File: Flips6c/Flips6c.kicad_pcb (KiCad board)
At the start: 2 copper layers, 90 x 50 mm, 20 parts, among them CN1 Conn_02x04_Odd_Even, U1 74HCT595, U2 74HCT595, U3 74HCT595

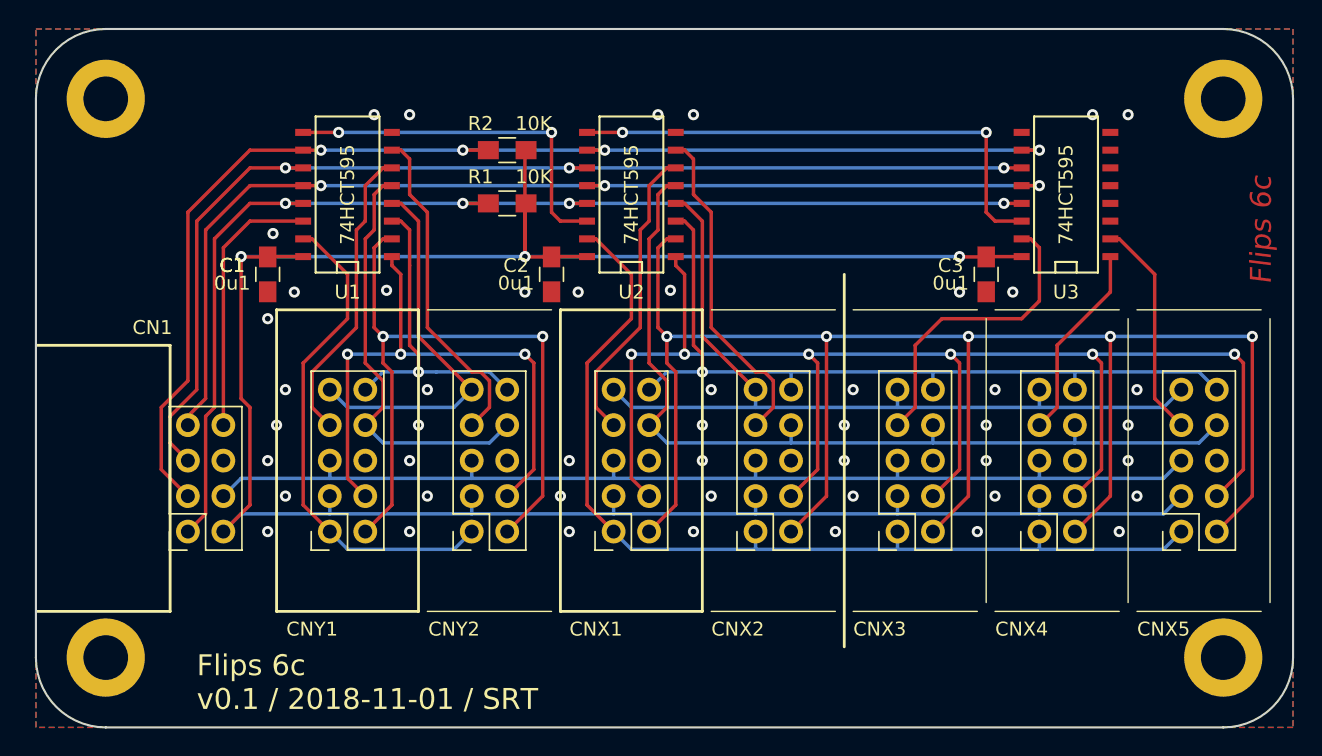
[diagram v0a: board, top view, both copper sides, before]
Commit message: changing trace widths
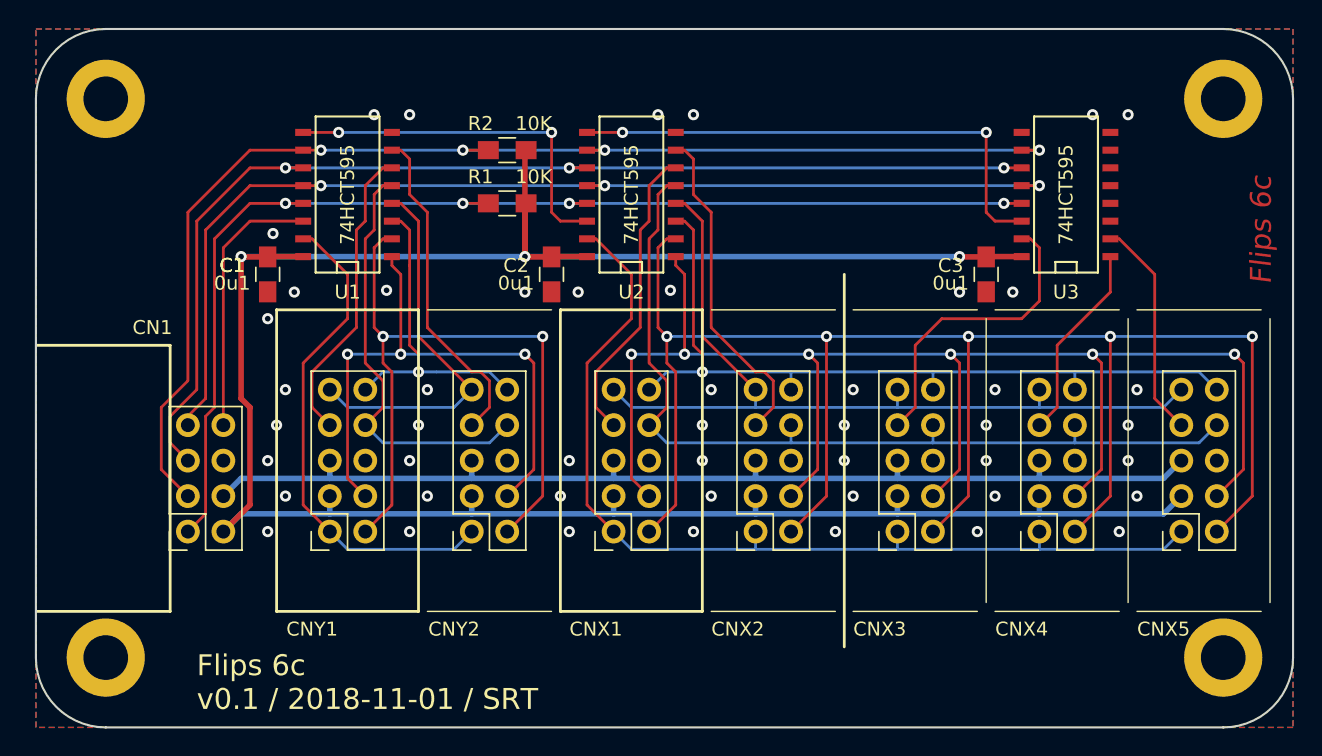
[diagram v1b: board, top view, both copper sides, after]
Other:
- net class Default: trace_width 0.25 -> 0.2
- net class POW added: clearance 0.2, trace_width 0.4, via_dia 0.8, via_drill 0.4

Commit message: flips 6c to use own UFP2810 connector
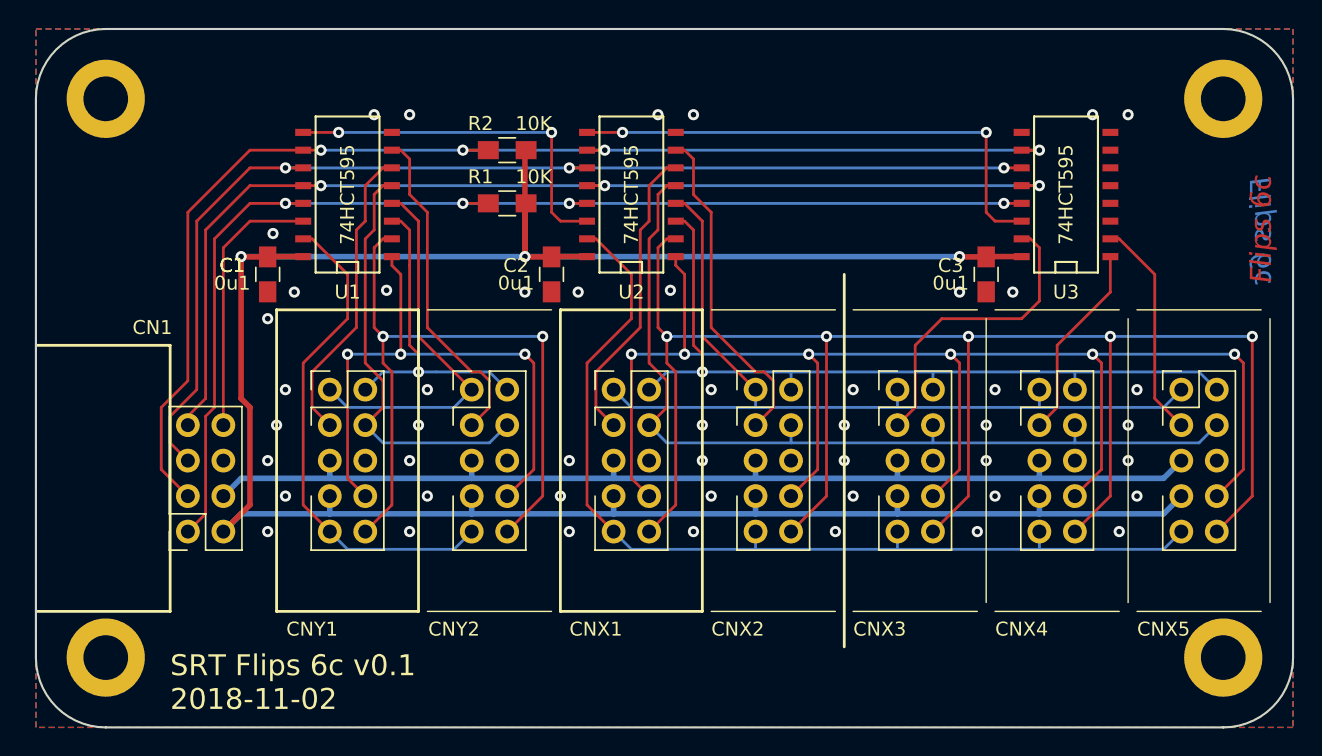
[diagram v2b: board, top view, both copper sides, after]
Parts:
- CNX1, CNX2, CNX3, CNX4, CNX5, CNY1, CNY2: value Conn_02x05_Odd_Even -> UFP2810; footprint Socket_Strips:Socket_Strip_Straight_2x05_Pitch2.54mm -> Own:Pin_Header_Straight_Shrouded_2x05_Pitch2.54mm
- moved CNX1 10.2 mm to (213.4, 83.8), turned to 0 degrees
- moved CNX2 10.2 mm to (223.5, 83.8), turned to 0 degrees
- moved CNX3 10.2 mm to (233.7, 83.8), turned to 0 degrees
- moved CNX4 10.2 mm to (243.8, 83.8), turned to 0 degrees
- moved CNX5 10.2 mm to (254.0, 83.8), turned to 0 degrees
- moved CNY1 10.2 mm to (193.0, 83.8), turned to 0 degrees
- moved CNY2 10.2 mm to (203.2, 83.8), turned to 0 degrees
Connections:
- CNX1 pad 1: /XA.0 -> /XB.1
- CNX1 pad 10: /XB.0 -> /XA.2
- CNX1 pad 2: /XA.2 -> /XB.0
- CNX1 pad 3: +5V -> /XEN1
- CNX1 pad 4: /XA.1 -> /XDAT
- CNX1 pad 7: /XEN1 -> +5V
- CNX1 pad 8: /XDAT -> /XA.1
- CNX1 pad 9: /XB.1 -> /XA.0
- CNX2 pad 1: /XA.0 -> /XB.1
- CNX2 pad 10: /XB.0 -> /XA.2
- CNX2 pad 2: /XA.2 -> /XB.0
- CNX2 pad 3: +5V -> /XEN2
- CNX2 pad 4: /XA.1 -> /XDAT
- CNX2 pad 7: /XEN2 -> +5V
- CNX2 pad 8: /XDAT -> /XA.1
- CNX2 pad 9: /XB.1 -> /XA.0
- CNX3 pad 1: /XA.0 -> /XB.1
- CNX3 pad 10: /XB.0 -> /XA.2
- CNX3 pad 2: /XA.2 -> /XB.0
- CNX3 pad 3: +5V -> /XEN3
- CNX3 pad 4: /XA.1 -> /XDAT
- CNX3 pad 7: /XEN3 -> +5V
- CNX3 pad 8: /XDAT -> /XA.1
- CNX3 pad 9: /XB.1 -> /XA.0
- CNX4 pad 1: /XA.0 -> /XB.1
- CNX4 pad 10: /XB.0 -> /XA.2
- CNX4 pad 2: /XA.2 -> /XB.0
- CNX4 pad 3: +5V -> /XEN4
- CNX4 pad 4: /XA.1 -> /XDAT
- CNX4 pad 7: /XEN4 -> +5V
- CNX4 pad 8: /XDAT -> /XA.1
- CNX4 pad 9: /XB.1 -> /XA.0
- CNX5 pad 1: /XA.0 -> /XB.1
- CNX5 pad 10: /XB.0 -> /XA.2
- CNX5 pad 2: /XA.2 -> /XB.0
- CNX5 pad 3: +5V -> /XEN5
- CNX5 pad 4: /XA.1 -> /XDAT
- CNX5 pad 7: /XEN5 -> +5V
- CNX5 pad 8: /XDAT -> /XA.1
- CNX5 pad 9: /XB.1 -> /XA.0
- CNY1 pad 1: /YA.0 -> /YB.1
- CNY1 pad 10: /YB.0 -> /YA.2
- CNY1 pad 2: /YA.2 -> /YB.0
- CNY1 pad 3: +5V -> /YEN1
- CNY1 pad 4: /YA.1 -> /YDAT
- CNY1 pad 7: /YEN1 -> +5V
- CNY1 pad 8: /YDAT -> /YA.1
- CNY1 pad 9: /YB.1 -> /YA.0
- CNY2 pad 1: /YA.0 -> /YB.1
- CNY2 pad 10: /YB.0 -> /YA.2
- CNY2 pad 2: /YA.2 -> /YB.0
- CNY2 pad 3: +5V -> /YEN2
- CNY2 pad 4: /YA.1 -> /YDAT
- CNY2 pad 7: /YEN2 -> +5V
- CNY2 pad 8: /YDAT -> /YA.1
- CNY2 pad 9: /YB.1 -> /YA.0
- U3 pad 3: (no net) -> /XEN6
- U3 pad 4: (no net) -> /XEN7
- U3 pad 5: (no net) -> /XEN8
- U3 pad 6: (no net) -> /YEN3
- U3 pad 7: (no net) -> /YEN4
- U3 pad 9: (no net) -> Net-(U3-Pad9)
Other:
- board text added: "SRT Flips 6c v0.1 2018-11-02"
- board text removed: "Flips 6c v0.1 / 2018-11-01 / SRT"

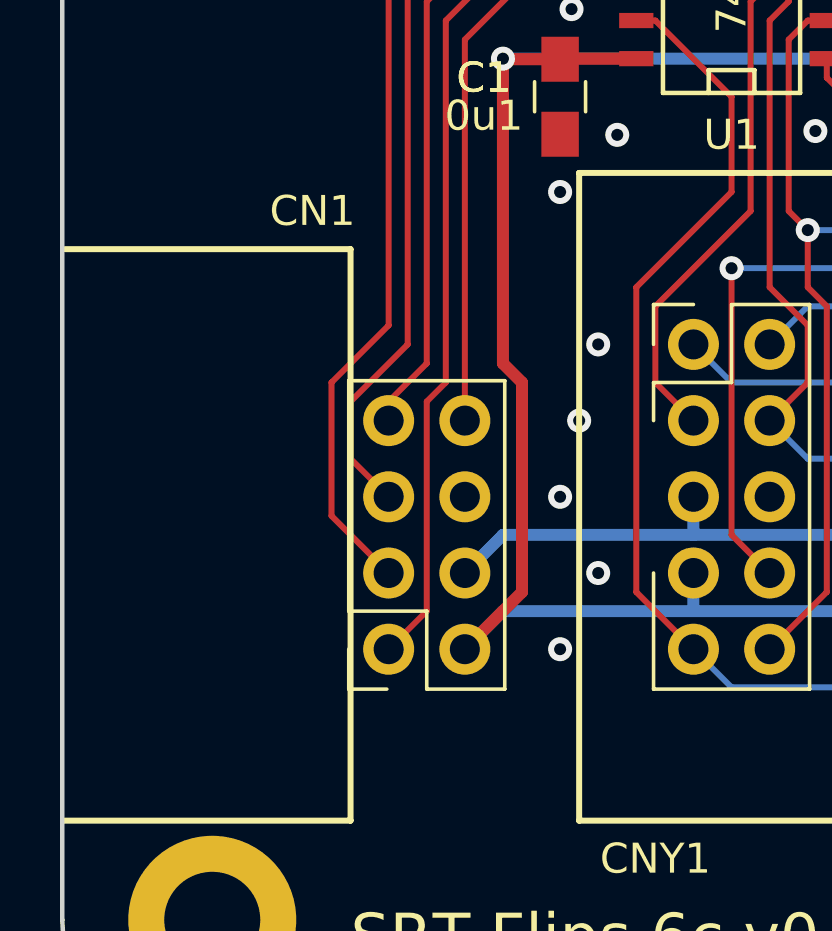
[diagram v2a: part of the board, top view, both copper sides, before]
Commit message: fixing 8 pin connector
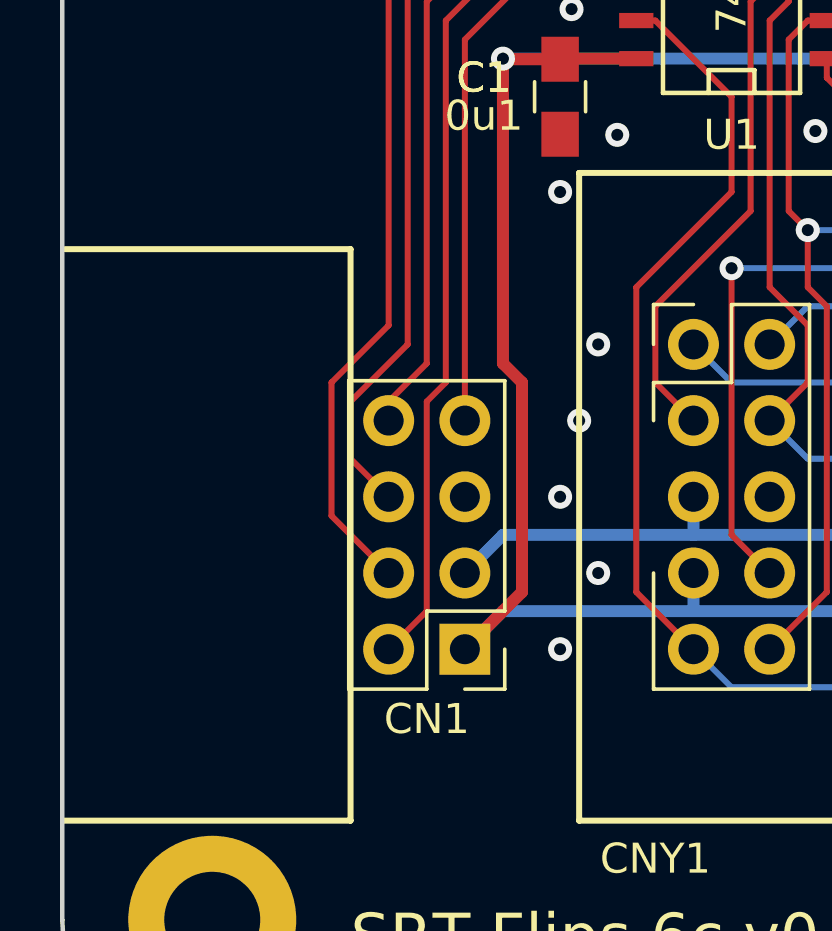
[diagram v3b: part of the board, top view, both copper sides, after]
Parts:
- CN1: footprint Socket_Strips:Socket_Strip_Straight_2x04_Pitch2.54mm -> Pin_Headers:Pin_Header_Straight_2x04_Pitch2.54mm
- moved CN1 2.54 mm to (185.4, 94.0)
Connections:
- CN1 pad 1: /~OE -> +5V
- CN1 pad 2: +5V -> /~OE
- CN1 pad 3: /~SRCLR -> +12V
- CN1 pad 4: +12V -> /~SRCLR
- CN1 pad 5: /SRCLK -> GND
- CN1 pad 6: GND -> /SRCLK
- CN1 pad 7: /RCLK -> /DIN
- CN1 pad 8: /DIN -> /RCLK
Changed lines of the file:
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@@
     (pad 1 thru_hole circle (at 0 0) (size 5.6 5.6) (drill 3.2) (layers *.Cu *.Mask))
-  )
-  (module Socket_Strips:Socket_Strip_Straight_2x04_Pitch2.54mm (layer F.Cu)
-    (at 182.88 93.98 180)
-    (descr "Through hole straight socket strip, 2x04, 2.54mm pitch, double rows")
-    (tags "Through hole socket strip THT 2x04 2.54mm double row")
-    (fp_text reference CN1 (at 2.54 14.605) (layer F.SilkS)
-      (effects (font (size 1 1) (thickness 0.15)))
-    )
-    (fp_text value Conn_02x04_Odd_Even (at -1.27 9.95 180) (layer F.Fab)
-      (effects (font (size 1 1) (thickness 0.15)))
-    )
-    (fp_text user %R (at 2.54 14.605 180) (layer F.Fab)
-      (effects (font (size 1 1) (thickness 0.15)))
-    )
-    (fp_line (start 1.8 -1.8) (end -4.35 -1.8) (layer F.CrtYd) (width 0.05))
-    (fp_line (start 1.8 9.4) (end 1.8 -1.8) (layer F.CrtYd) (width 0.05))
-    (fp_line (start -4.35 9.4) (end 1.8 9.4) (layer F.CrtYd) (width 0.05))
-    (fp_line (start -4.35 -1.8) (end -4.35 9.4) (layer F.CrtYd) (width 0.05))
-    (fp_line (start 1.33 -1.33) (end 0.06 -1.33) (layer F.SilkS) (width 0.12))
-    (fp_line (start 1.33 0) (end 1.33 -1.33) (layer F.SilkS) (width 0.12))
-    (fp_line (start -1.27 1.27) (end 1.33 1.27) (layer F.SilkS) (width 0.12))
-    (fp_line (start -1.27 -1.33) (end -1.27 1.27) (layer F.SilkS) (width 0.12))
-    (fp_line (start -3.87 -1.33) (end -1.27 -1.33) (layer F.SilkS) (width 0.12))
-    (fp_line (start -3.87 8.95) (end -3.87 -1.33) (layer F.SilkS) (width 0.12))
-    (fp_line (start 1.33 8.95) (end -3.87 8.95) (layer F.SilkS) (width 0.12))
-    (fp_line (start 1.33 1.27) (end 1.33 8.95) (layer F.SilkS) (width 0.12))
-    (fp_line (start 1.27 -1.27) (end -3.81 -1.27) (layer F.Fab) (width 0.1))
-    (fp_line (start 1.27 8.89) (end 1.27 -1.27) (layer F.Fab) (width 0.1))
-    (fp_line (start -3.81 8.89) (end 1.27 8.89) (layer F.Fab) (width 0.1))
-    (fp_line (start -3.81 -1.27) (end -3.81 8.89) (layer F.Fab) (width 0.1))
-    (pad 8 thru_hole oval (at -2.54 7.62 180) (size 1.7 1.7) (drill 1) (layers *.Cu *.Mask)
-      (net 4 /DIN))
-    (pad 7 thru_hole oval (at 0 7.62 180) (size 1.7 1.7) (drill 1) (layers *.Cu *.Mask)
-      (net 5 /RCLK))
-    (pad 6 thru_hole oval (at -2.54 5.08 180) (size 1.7 1.7) (drill 1) (layers *.Cu *.Mask)
-      (net 2 GND))
-    (pad 5 thru_hole oval (at 0 5.08 180) (size 1.7 1.7) (drill 1) (layers *.Cu *.Mask)
-      (net 6 /SRCLK))
-    (pad 4 thru_hole oval (at -2.54 2.54 180) (size 1.7 1.7) (drill 1) (layers *.Cu *.Mask)
-      (net 3 +12V))
-    (pad 3 thru_hole oval (at 0 2.54 180) (size 1.7 1.7) (drill 1) (layers *.Cu *.Mask)
-      (net 7 /~SRCLR))
-    (pad 2 thru_hole oval (at -2.54 0 180) (size 1.7 1.7) (drill 1) (layers *.Cu *.Mask)
-      (net 1 +5V))
-    (pad 1 thru_hole circle (at 0 0 180) (size 1.7 1.7) (drill 1) (layers *.Cu *.Mask)
-      (net 9 /~OE))
-    (model ${KISYS3DMOD}/Connector_IDC.3dshapes/IDC-Header_2x04_P2.54mm_Horizontal.wrl
-      (offset (xyz -2.54 0 0))
-      (scale (xyz 1 1 1))
-      (rotate (xyz 0 0 0))
-    )
   )
   (module Capacitors_SMD:C_0805_HandSoldering (layer F.Cu)
@@
       (at (xyz 0 0 0))
       (scale (xyz 1 1 1))
+      (rotate (xyz 0 0 0))
+    )
+  )
+  (module Pin_Headers:Pin_Header_Straight_2x04_Pitch2.54mm (layer F.Cu)
+    (at 185.42 93.98 180)
+    (descr "Through hole straight pin header, 2x04, 2.54mm pitch, double rows")
+    (tags "Through hole pin header THT 2x04 2.54mm double row")
+    (fp_text reference CN1 (at 1.27 -2.33 180) (layer F.SilkS)
+      (effects (font (size 1 1) (thickness 0.15)))
+    )
+    (fp_text value Conn_02x04_Odd_Even (at 1.27 9.95 180) (layer F.Fab)
+      (effects (font (size 1 1) (thickness 0.15)))
+    )
+    (fp_text user %R (at 1.27 3.81 270) (layer F.Fab)
+      (effects (font (size 1 1) (thickness 0.15)))
+    )
+    (fp_line (start 4.35 -1.8) (end -1.8 -1.8) (layer F.CrtYd) (width 0.05))
+    (fp_line (start 4.35 9.4) (end 4.35 -1.8) (layer F.CrtYd) (width 0.05))
+    (fp_line (start -1.8 9.4) (end 4.35 9.4) (layer F.CrtYd) (width 0.05))
+    (fp_line (start -1.8 -1.8) (end -1.8 9.4) (layer F.CrtYd) (width 0.05))
+    (fp_line (start -1.33 -1.33) (end 0 -1.33) (layer F.SilkS) (width 0.12))
+    (fp_line (start -1.33 0) (end -1.33 -1.33) (layer F.SilkS) (width 0.12))
+    (fp_line (start 1.27 -1.33) (end 3.87 -1.33) (layer F.SilkS) (width 0.12))
+    (fp_line (start 1.27 1.27) (end 1.27 -1.33) (layer F.SilkS) (width 0.12))
+    (fp_line (start -1.33 1.27) (end 1.27 1.27) (layer F.SilkS) (width 0.12))
+    (fp_line (start 3.87 -1.33) (end 3.87 8.95) (layer F.SilkS) (width 0.12))
+    (fp_line (start -1.33 1.27) (end -1.33 8.95) (layer F.SilkS) (width 0.12))
+    (fp_line (start -1.33 8.95) (end 3.87 8.95) (layer F.SilkS) (width 0.12))
+    (fp_line (start -1.27 0) (end 0 -1.27) (layer F.Fab) (width 0.1))
+    (fp_line (start -1.27 8.89) (end -1.27 0) (layer F.Fab) (width 0.1))
+    (fp_line (start 3.81 8.89) (end -1.27 8.89) (layer F.Fab) (width 0.1))
+    (fp_line (start 3.81 -1.27) (end 3.81 8.89) (layer F.Fab) (width 0.1))
+    (fp_line (start 0 -1.27) (end 3.81 -1.27) (layer F.Fab) (width 0.1))
+    (pad 8 thru_hole oval (at 2.54 7.62 180) (size 1.7 1.7) (drill 1) (layers *.Cu *.Mask)
+      (net 5 /RCLK))
+    (pad 7 thru_hole oval (at 0 7.62 180) (size 1.7 1.7) (drill 1) (layers *.Cu *.Mask)
+      (net 4 /DIN))
+    (pad 6 thru_hole oval (at 2.54 5.08 180) (size 1.7 1.7) (drill 1) (layers *.Cu *.Mask)
+      (net 6 /SRCLK))
+    (pad 5 thru_hole oval (at 0 5.08 180) (size 1.7 1.7) (drill 1) (layers *.Cu *.Mask)
+      (net 2 GND))
+    (pad 4 thru_hole oval (at 2.54 2.54 180) (size 1.7 1.7) (drill 1) (layers *.Cu *.Mask)
+      (net 7 /~SRCLR))
+    (pad 3 thru_hole oval (at 0 2.54 180) (size 1.7 1.7) (drill 1) (layers *.Cu *.Mask)
+      (net 3 +12V))
+    (pad 2 thru_hole oval (at 2.54 0 180) (size 1.7 1.7) (drill 1) (layers *.Cu *.Mask)
+      (net 9 /~OE))
+    (pad 1 thru_hole rect (at 0 0 180) (size 1.7 1.7) (drill 1) (layers *.Cu *.Mask)
+      (net 1 +5V))
+    (model ${KISYS3DMOD}/Connector_IDC.3dshapes/IDC-Header_2x04_P2.54mm_Horizontal.wrl
+      (at (xyz 0 0 0))
+      (scale (xyz 1 1 1))

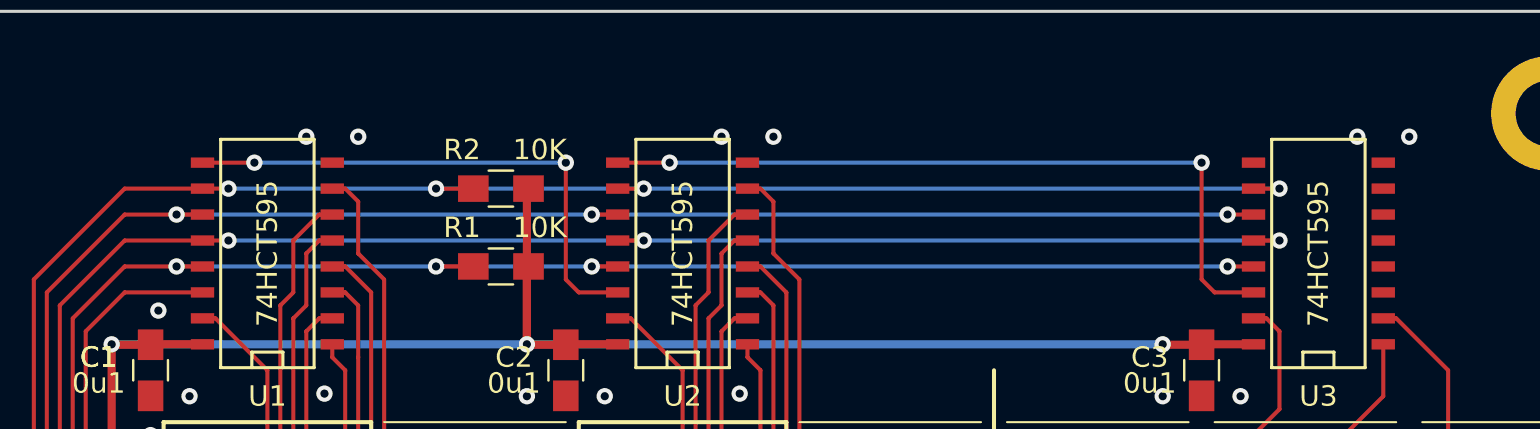
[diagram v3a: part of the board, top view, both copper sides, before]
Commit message: improve 595 control traces
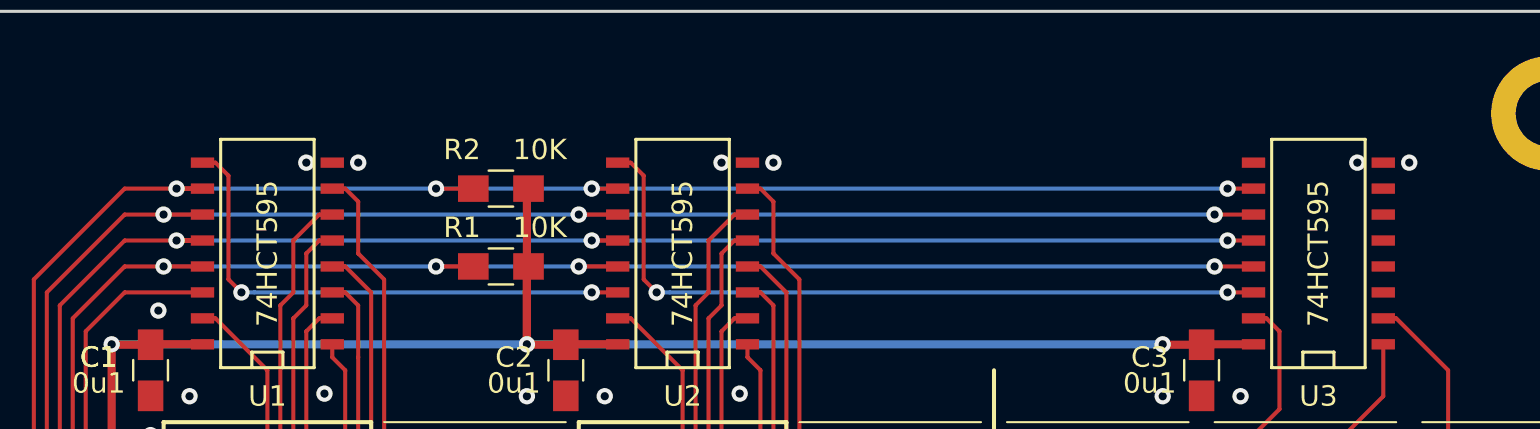
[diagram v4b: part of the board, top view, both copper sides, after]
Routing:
- net /~OE: track 84.9 -> 86.2 mm
- net /SRCLK: track 81.6 -> 82.9 mm
